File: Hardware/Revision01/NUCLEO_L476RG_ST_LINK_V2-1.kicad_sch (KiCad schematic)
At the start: 70 parts, among them CN10 Header 4, CN7 5075BMR-05-SM, CN9 Header 6X1, T2 9013, U12 STM32F103CBT6, U13 LD3985M33R, X1 8MHz(12pF)

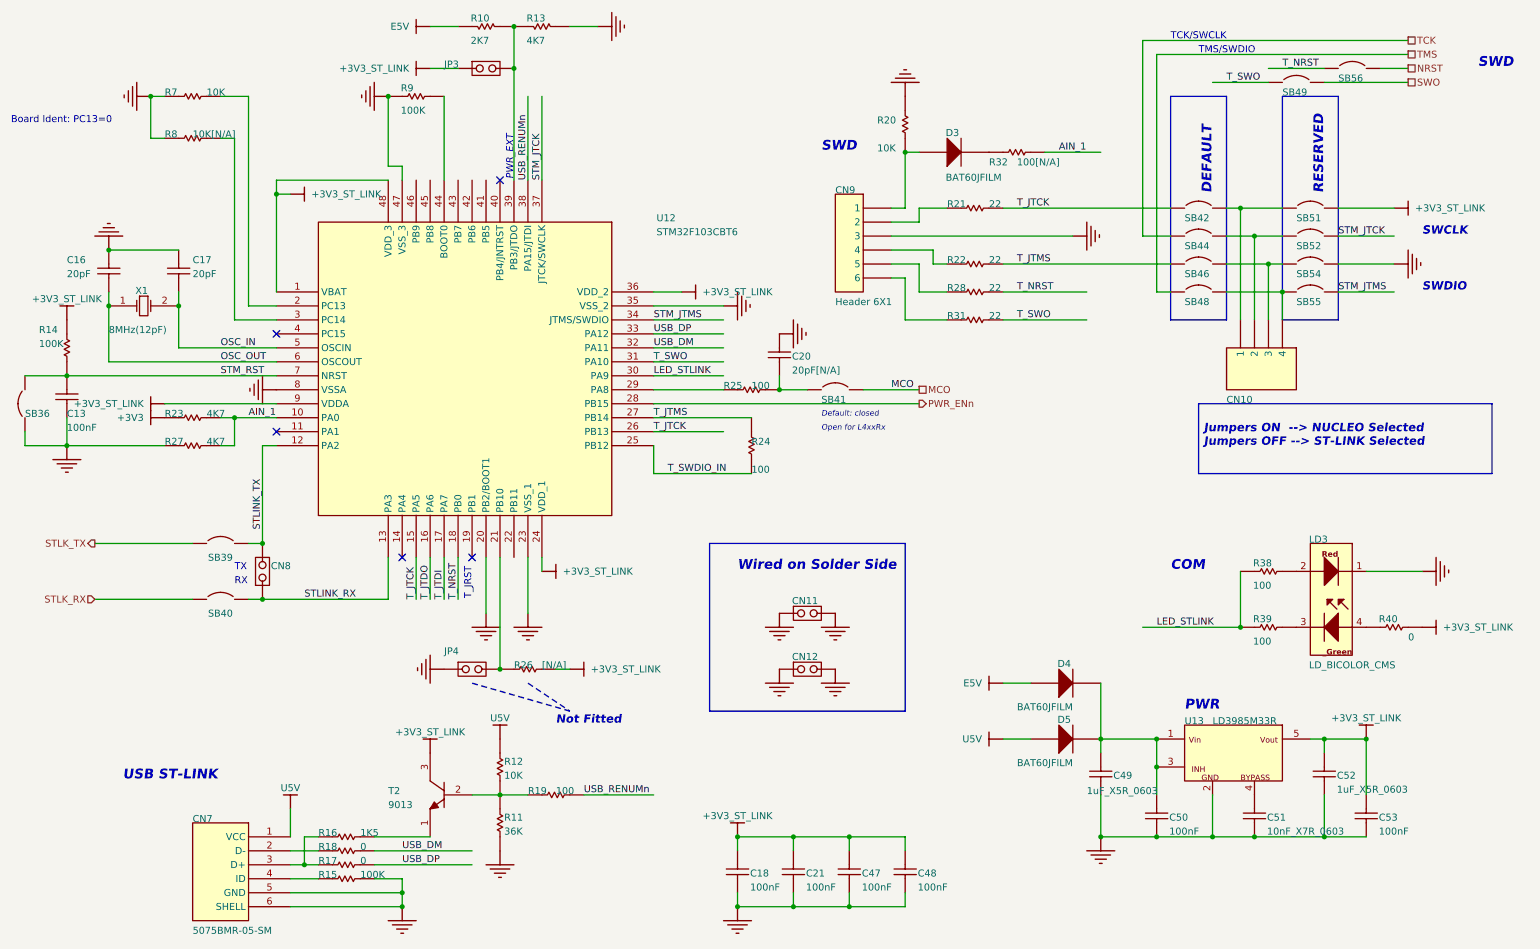
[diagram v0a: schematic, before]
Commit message: . Renamed schematic files, removed old symbol files
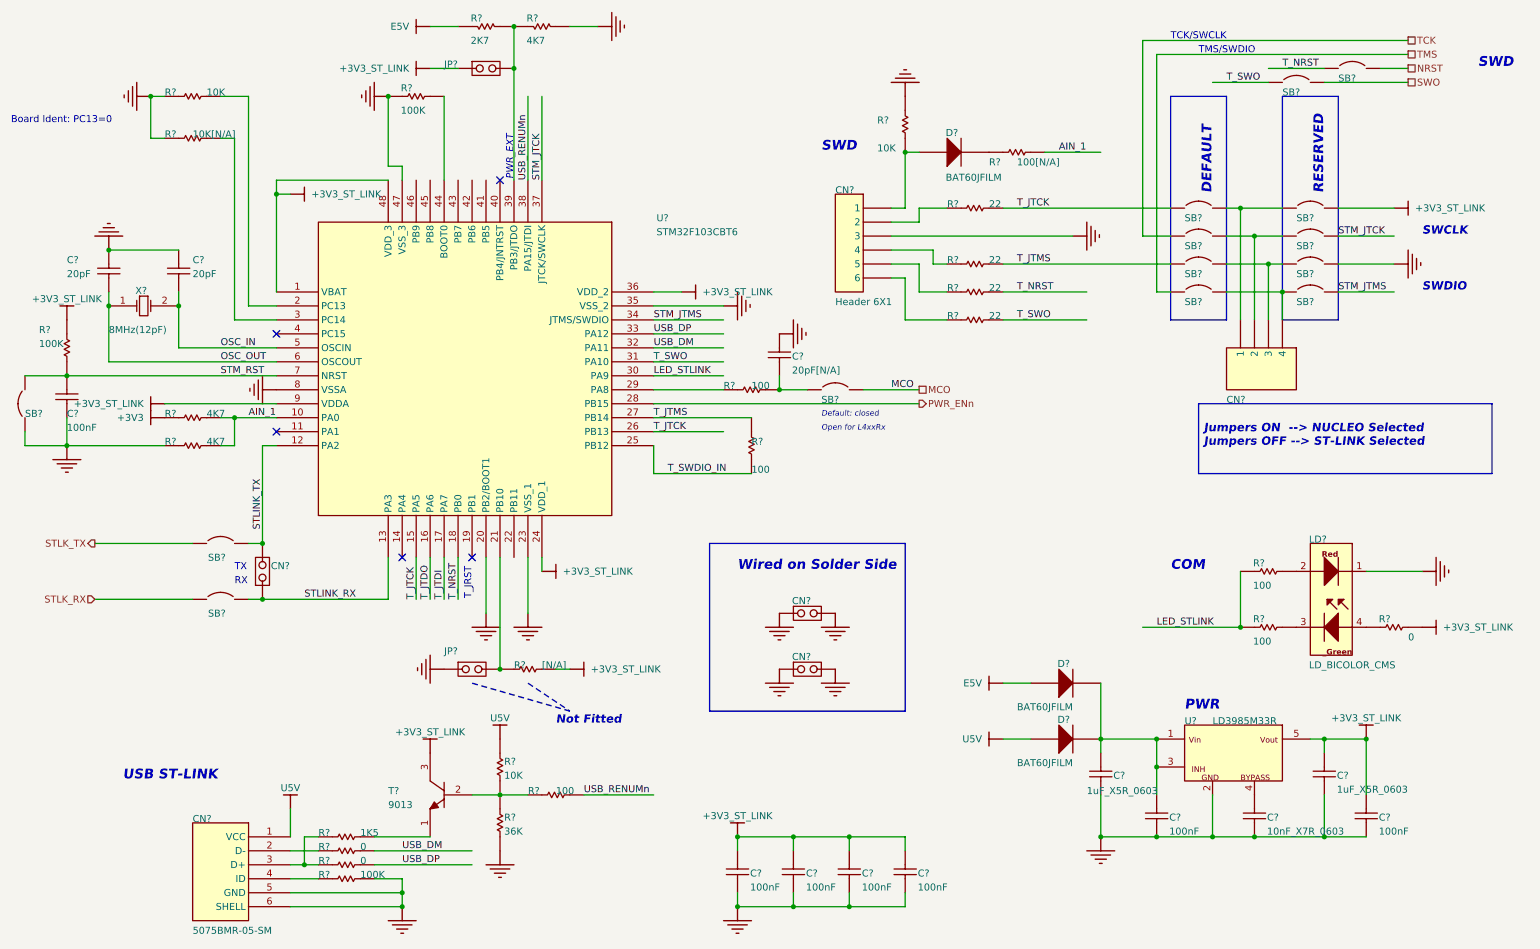
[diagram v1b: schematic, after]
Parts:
- renumbered C48 to C?, C52 to C?, C17 to C?, C47 to C?, C49 to C?, C13 to C?, C16 to C?, C18 to C?, C50 to C?, C20 to C?, C21 to C?, C53 to C?, C51 to C?, CN9 to CN?, CN12 to CN?, CN7 to CN?, CN11 to CN?, CN8 to CN?, CN10 to CN?, D4 to D?, D5 to D?, D3 to D?, JP3 to JP?, JP4 to JP?, LD3 to LD?, R10 to R?, R25 to R?, R15 to R?, R21 to R?, R24 to R?, R18 to R?, R19 to R?, R27 to R?, R7 to R?, R40 to R?, R9 to R?, R14 to R?, R28 to R?, R20 to R?, R11 to R?, R8 to R?, R22 to R?, R17 to R?, R39 to R?, R31 to R?, R38 to R?, R23 to R?, R16 to R?, R26 to R?, R12 to R?, R32 to R?, R13 to R?, SB44 to SB?, SB42 to SB?, SB39 to SB?, SB52 to SB?, SB51 to SB?, SB40 to SB?, SB36 to SB?, SB54 to SB?, SB55 to SB?, SB49 to SB?, SB41 to SB?, SB48 to SB?, SB56 to SB?, SB46 to SB?, T2 to T?, U13 to U?, U12 to U?, X1 to X?

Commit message: . Completed MCU schematic & imported hierarchical model pins
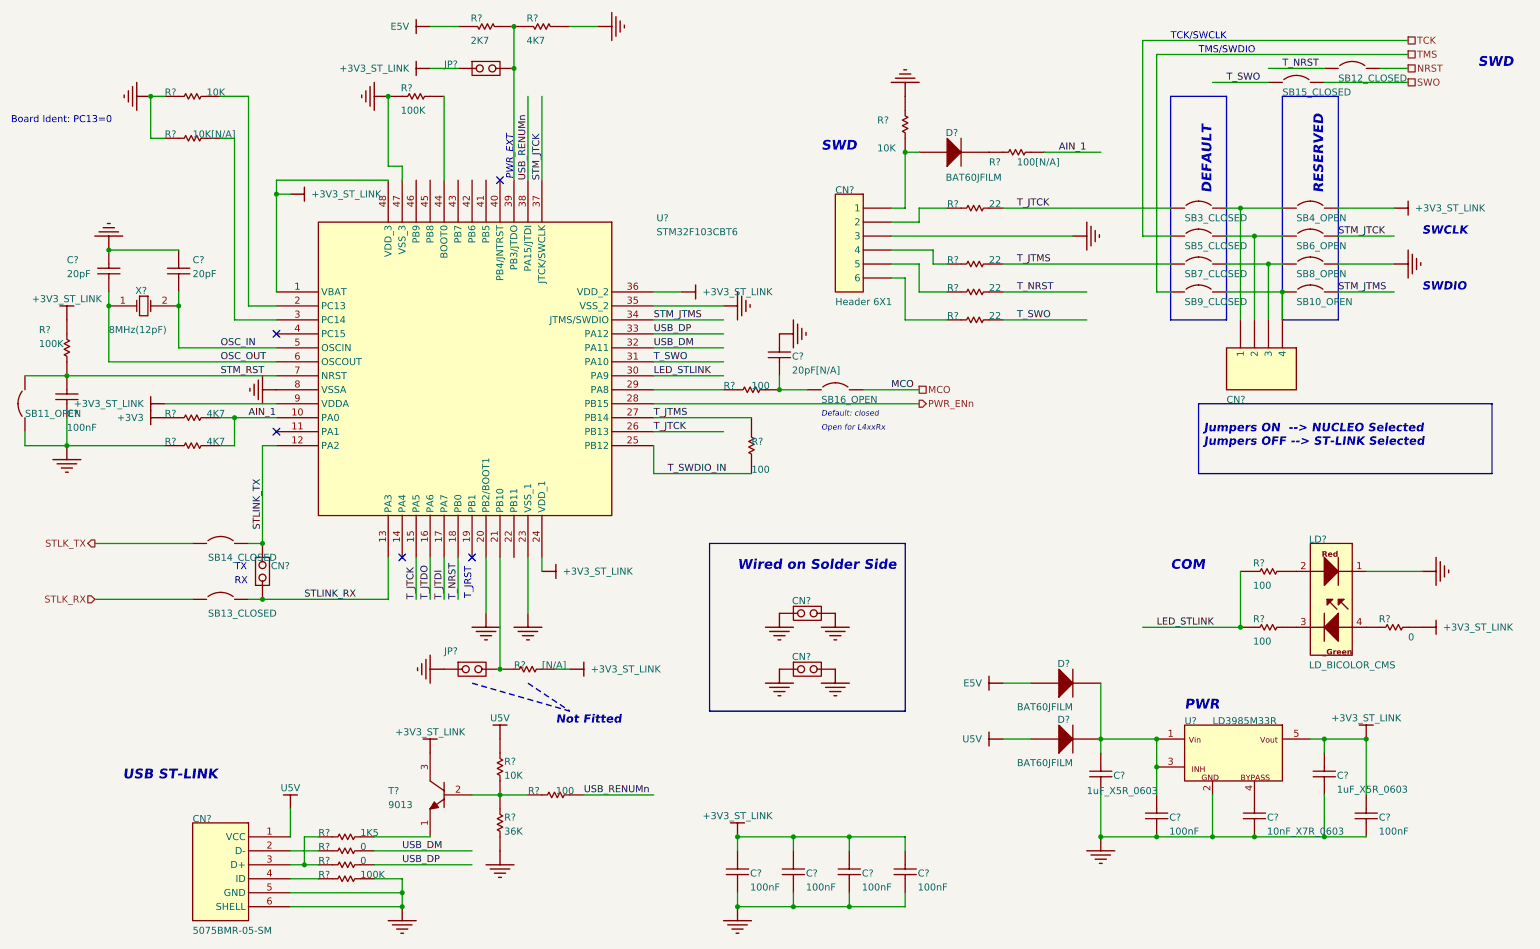
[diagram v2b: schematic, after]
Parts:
- gave numbers to parts that had none: 14
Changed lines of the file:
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@@
 		(on_board yes)
 		(dnp no)
-		(property "Reference" "SB?"
+		(property "Reference" "SB5_CLOSED"
 			(at 226.06 54.61 0)
 			(effects
@@
 			(project "Revision01"
 				(path "/955cc99e-a129-42cf-abc7-aa99813fdb5f/00000000-0000-0000-0000-00005ea70ac3/dfd3e576-45ac-414e-879c-fe3a4e293d3a/64cd4bef-5636-43e4-afe9-e13f95815028"
-					(reference "SB?")
+					(reference "SB5_CLOSED")
 					(unit 1)
 				)
@@
 		(on_board yes)
 		(dnp no)
-		(property "Reference" "SB?"
+		(property "Reference" "SB3_CLOSED"
 			(at 226.06 49.53 0)
 			(effects
@@
 			(project "Revision01"
 				(path "/955cc99e-a129-42cf-abc7-aa99813fdb5f/00000000-0000-0000-0000-00005ea70ac3/dfd3e576-45ac-414e-879c-fe3a4e293d3a/64cd4bef-5636-43e4-afe9-e13f95815028"
-					(reference "SB?")
+					(reference "SB3_CLOSED")
 					(unit 1)
 				)
@@
 		(on_board yes)
 		(dnp no)
-		(property "Reference" "SB?"
+		(property "Reference" "SB14_CLOSED"
 			(at 48.514 111.252 0)
 			(effects
@@
 			(project "Revision01"
 				(path "/955cc99e-a129-42cf-abc7-aa99813fdb5f/00000000-0000-0000-0000-00005ea70ac3/dfd3e576-45ac-414e-879c-fe3a4e293d3a/64cd4bef-5636-43e4-afe9-e13f95815028"
-					(reference "SB?")
+					(reference "SB14_CLOSED")
 					(unit 1)
 				)
@@
 		(on_board yes)
 		(dnp no)
-		(property "Reference" "SB?"
+		(property "Reference" "SB6_OPEN"
 			(at 246.38 54.61 0)
 			(effects
@@
 			(project "Revision01"
 				(path "/955cc99e-a129-42cf-abc7-aa99813fdb5f/00000000-0000-0000-0000-00005ea70ac3/dfd3e576-45ac-414e-879c-fe3a4e293d3a/64cd4bef-5636-43e4-afe9-e13f95815028"
-					(reference "SB?")
+					(reference "SB6_OPEN")
 					(unit 1)
 				)
@@
 		(on_board yes)
 		(dnp no)
-		(property "Reference" "SB?"
+		(property "Reference" "SB4_OPEN"
 			(at 246.38 49.53 0)
 			(effects
@@
 			(project "Revision01"
 				(path "/955cc99e-a129-42cf-abc7-aa99813fdb5f/00000000-0000-0000-0000-00005ea70ac3/dfd3e576-45ac-414e-879c-fe3a4e293d3a/64cd4bef-5636-43e4-afe9-e13f95815028"
-					(reference "SB?")
+					(reference "SB4_OPEN")
 					(unit 1)
 				)
@@
 		(on_board yes)
 		(dnp no)
-		(property "Reference" "SB?"
+		(property "Reference" "SB13_CLOSED"
 			(at 48.514 121.412 0)
 			(effects
@@
 			(project "Revision01"
 				(path "/955cc99e-a129-42cf-abc7-aa99813fdb5f/00000000-0000-0000-0000-00005ea70ac3/dfd3e576-45ac-414e-879c-fe3a4e293d3a/64cd4bef-5636-43e4-afe9-e13f95815028"
-					(reference "SB?")
+					(reference "SB13_CLOSED")
 					(unit 1)
 				)
@@
 		(on_board yes)
 		(dnp no)
-		(property "Reference" "SB?"
+		(property "Reference" "SB11_OPEN"
 			(at 15.24 85.09 0)
 			(effects
@@
 			(project "Revision01"
 				(path "/955cc99e-a129-42cf-abc7-aa99813fdb5f/00000000-0000-0000-0000-00005ea70ac3/dfd3e576-45ac-414e-879c-fe3a4e293d3a/64cd4bef-5636-43e4-afe9-e13f95815028"
-					(reference "SB?")
+					(reference "SB11_OPEN")
 					(unit 1)
 				)
@@
 		(on_board yes)
 		(dnp no)
-		(property "Reference" "SB?"
+		(property "Reference" "SB8_OPEN"
 			(at 246.38 59.69 0)
 			(effects
@@
 			(project "Revision01"
 				(path "/955cc99e-a129-42cf-abc7-aa99813fdb5f/00000000-0000-0000-0000-00005ea70ac3/dfd3e576-45ac-414e-879c-fe3a4e293d3a/64cd4bef-5636-43e4-afe9-e13f95815028"
-					(reference "SB?")
+					(reference "SB8_OPEN")
 					(unit 1)
 				)
@@
 		(on_board yes)
 		(dnp no)
-		(property "Reference" "SB?"
+		(property "Reference" "SB10_OPEN"
 			(at 246.38 64.77 0)
 			(effects
@@
 			(project "Revision01"
 				(path "/955cc99e-a129-42cf-abc7-aa99813fdb5f/00000000-0000-0000-0000-00005ea70ac3/dfd3e576-45ac-414e-879c-fe3a4e293d3a/64cd4bef-5636-43e4-afe9-e13f95815028"
-					(reference "SB?")
+					(reference "SB10_OPEN")
 					(unit 1)
 				)
@@
 		(on_board yes)
 		(dnp no)
-		(property "Reference" "SB?"
+		(property "Reference" "SB15_CLOSED"
 			(at 243.84 26.67 0)
 			(effects
@@
 			(project "Revision01"
 				(path "/955cc99e-a129-42cf-abc7-aa99813fdb5f/00000000-0000-0000-0000-00005ea70ac3/dfd3e576-45ac-414e-879c-fe3a4e293d3a/64cd4bef-5636-43e4-afe9-e13f95815028"
-					(reference "SB?")
+					(reference "SB15_CLOSED")
 					(unit 1)
 				)
@@
 		(on_board yes)
 		(dnp no)
-		(property "Reference" "SB?"
+		(property "Reference" "SB16_OPEN"
 			(at 160.02 82.55 0)
 			(effects
@@
 			(project "Revision01"
 				(path "/955cc99e-a129-42cf-abc7-aa99813fdb5f/00000000-0000-0000-0000-00005ea70ac3/dfd3e576-45ac-414e-879c-fe3a4e293d3a/64cd4bef-5636-43e4-afe9-e13f95815028"
-					(reference "SB?")
+					(reference "SB16_OPEN")
 					(unit 1)
 				)
@@
 		(on_board yes)
 		(dnp no)
-		(property "Reference" "SB?"
+		(property "Reference" "SB9_CLOSED"
 			(at 226.06 64.77 0)
 			(effects
@@
 			(project "Revision01"
 				(path "/955cc99e-a129-42cf-abc7-aa99813fdb5f/00000000-0000-0000-0000-00005ea70ac3/dfd3e576-45ac-414e-879c-fe3a4e293d3a/64cd4bef-5636-43e4-afe9-e13f95815028"
-					(reference "SB?")
+					(reference "SB9_CLOSED")
 					(unit 1)
 				)
@@
 		(on_board yes)
 		(dnp no)
-		(property "Reference" "SB?"
+		(property "Reference" "SB12_CLOSED"
 			(at 254 24.13 0)
 			(effects
@@
 			(project "Revision01"
 				(path "/955cc99e-a129-42cf-abc7-aa99813fdb5f/00000000-0000-0000-0000-00005ea70ac3/dfd3e576-45ac-414e-879c-fe3a4e293d3a/64cd4bef-5636-43e4-afe9-e13f95815028"
-					(reference "SB?")
+					(reference "SB12_CLOSED")
 					(unit 1)
 				)
@@
 		(on_board yes)
 		(dnp no)
-		(property "Reference" "SB?"
+		(property "Reference" "SB7_CLOSED"
 			(at 226.06 59.69 0)
 			(effects
@@
 			(project "Revision01"
 				(path "/955cc99e-a129-42cf-abc7-aa99813fdb5f/00000000-0000-0000-0000-00005ea70ac3/dfd3e576-45ac-414e-879c-fe3a4e293d3a/64cd4bef-5636-43e4-afe9-e13f95815028"
-					(reference "SB?")
+					(reference "SB7_CLOSED")
 					(unit 1)
 				)

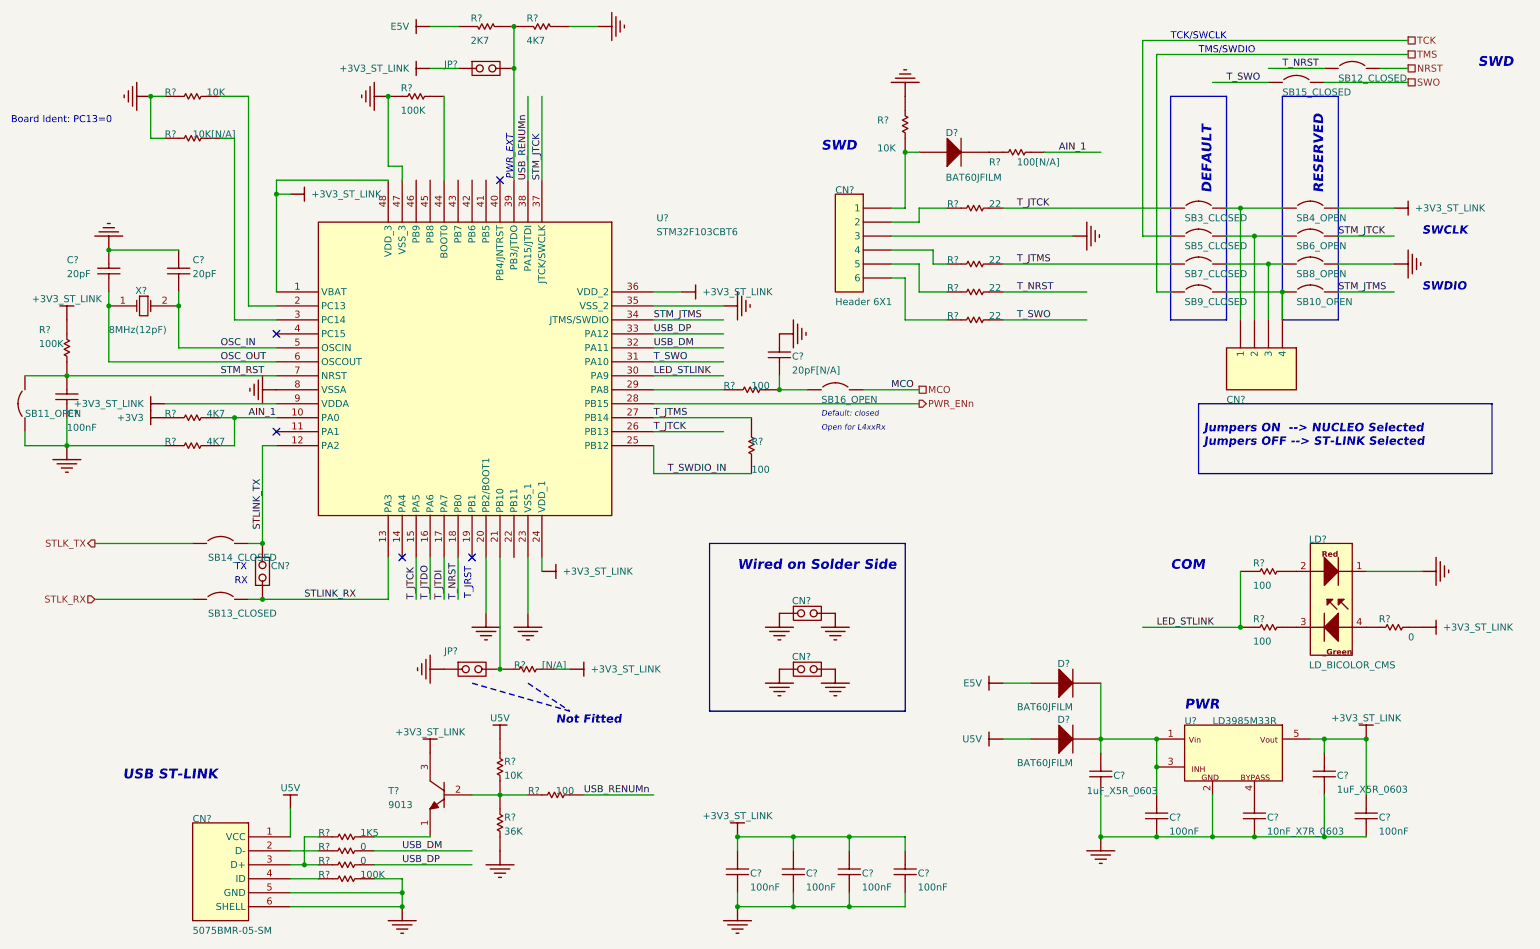
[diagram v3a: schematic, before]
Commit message: CREATE STM32CUBEIDE file to verify all ports Check over CONTROLLER SHEET Improve annotation ordering Move testpoints out of controller sheet
Still performering ERC check
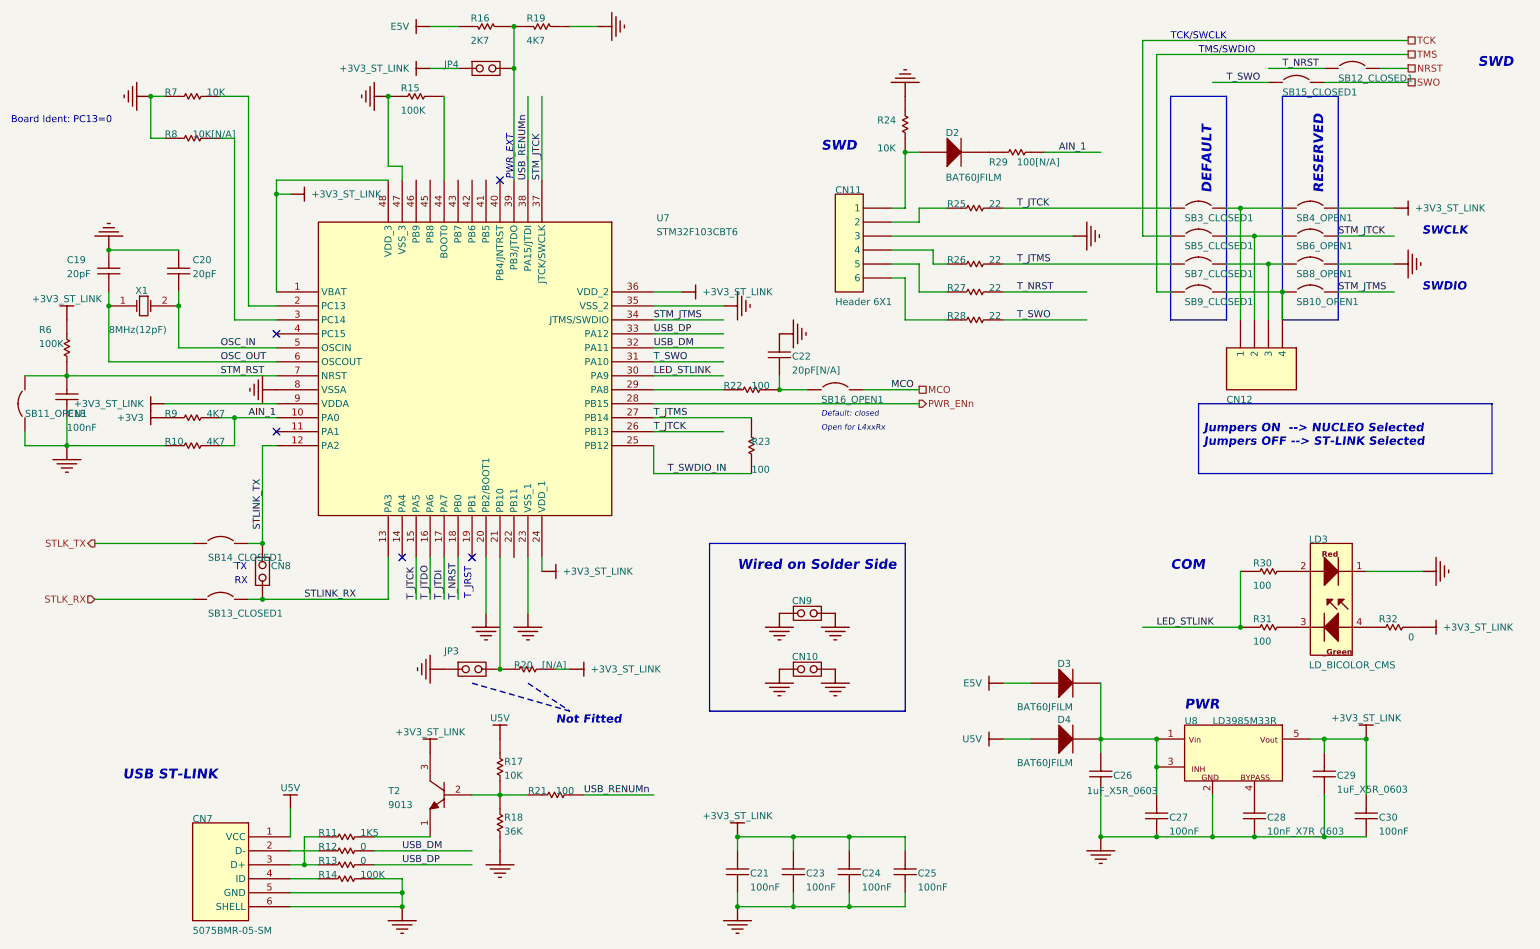
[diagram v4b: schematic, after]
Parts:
- gave numbers to parts that had none: 56
- renumbered SB10_OPEN to SB10_OPEN1, SB11_OPEN to SB11_OPEN1, SB12_CLOSED to SB12_CLOSED1, SB13_CLOSED to SB13_CLOSED1, SB14_CLOSED to SB14_CLOSED1, SB15_CLOSED to SB15_CLOSED1, SB16_OPEN to SB16_OPEN1, SB3_CLOSED to SB3_CLOSED1, SB4_OPEN to SB4_OPEN1, SB5_CLOSED to SB5_CLOSED1, SB6_OPEN to SB6_OPEN1, SB7_CLOSED to SB7_CLOSED1, SB8_OPEN to SB8_OPEN1, SB9_CLOSED to SB9_CLOSED1
